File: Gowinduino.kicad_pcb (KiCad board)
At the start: 2 copper layers, 68.6 x 53.3 mm, 9 parts, among them J1 Power, J2 Analog, J3 Digital, J4 Digital, J5 SPI

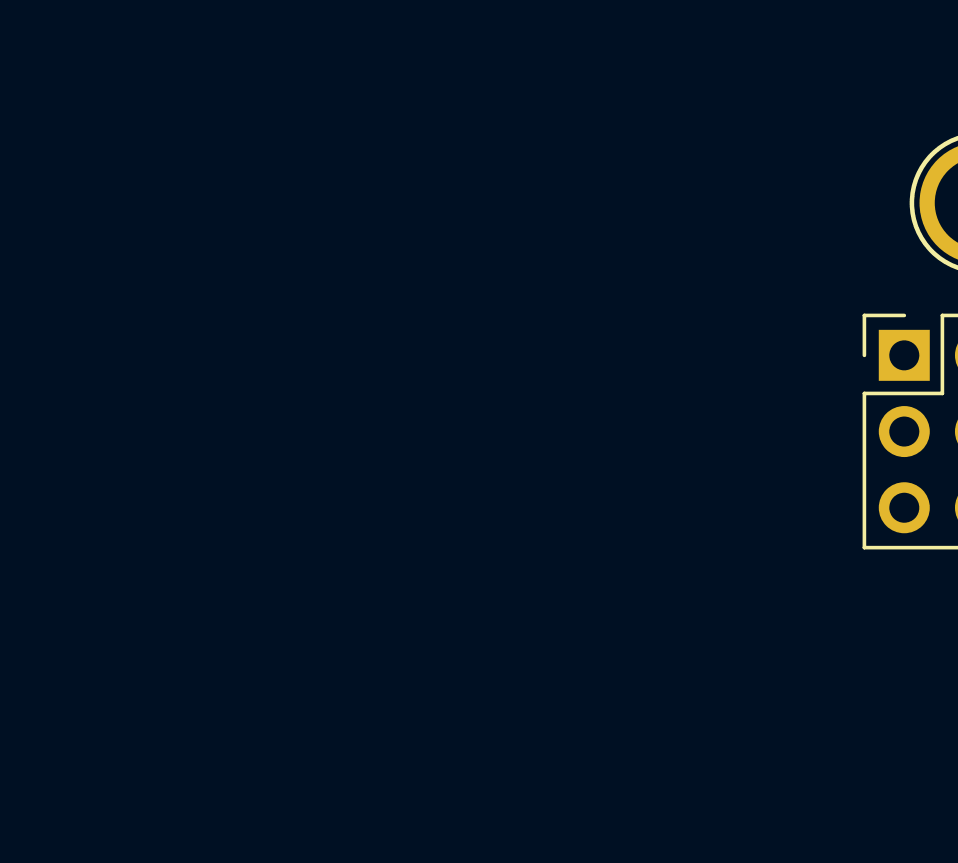
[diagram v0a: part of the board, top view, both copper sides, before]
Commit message: PCB: Introduced FPGA and SPI Flash
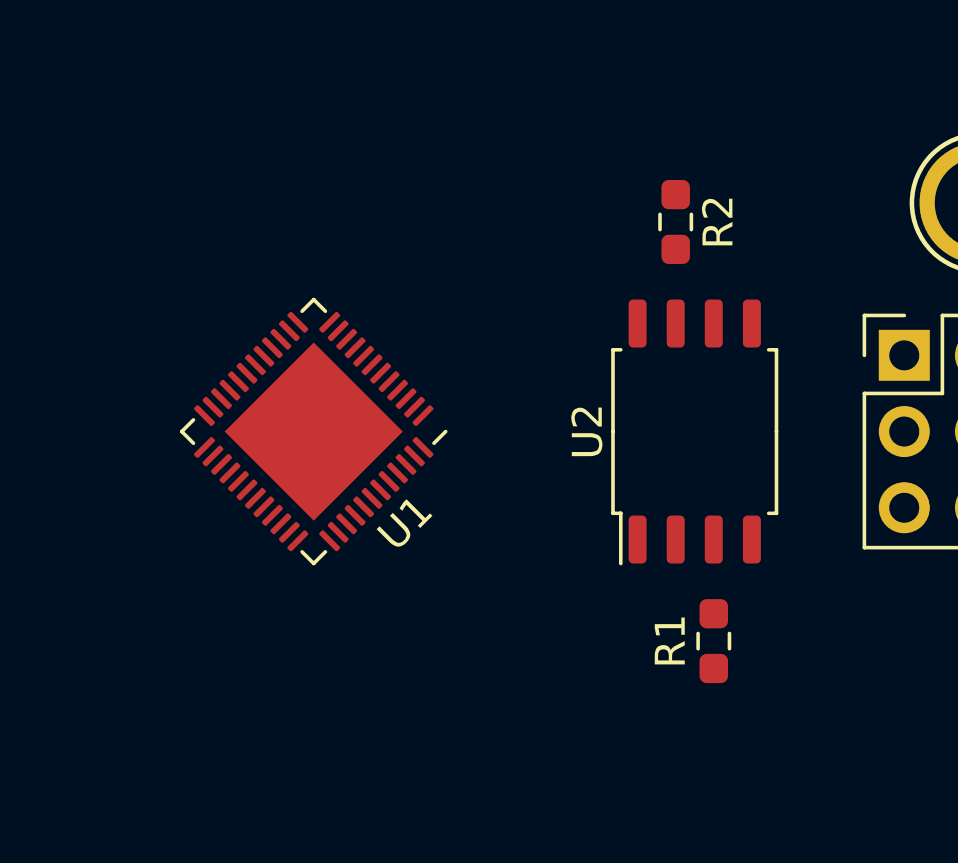
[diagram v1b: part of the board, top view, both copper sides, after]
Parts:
- added R1: 10k, Resistor_SMD:R_0603_1608Metric_Pad0.98x0.95mm_HandSolder, F.Cu at (168.1, 105.4)
- added R2: 10k, Resistor_SMD:R_0603_1608Metric_Pad0.98x0.95mm_HandSolder, F.Cu at (166.9, 91.4)
- added U1: GW1NSR-4CQN48P, Package_DFN_QFN:QFN-48-1EP_6x6mm_P0.4mm_EP4.2x4.2mm, F.Cu at (154.8, 98.4)
- added U2: W25Q32JVSS, Package_SO:SOIC-8_5.23x5.23mm_P1.27mm, F.Cu at (167.5, 98.4)
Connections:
- J5 pad 1: (no net) -> /MISO
- J5 pad 3: (no net) -> /SCLK
- J5 pad 4: (no net) -> /MOSI

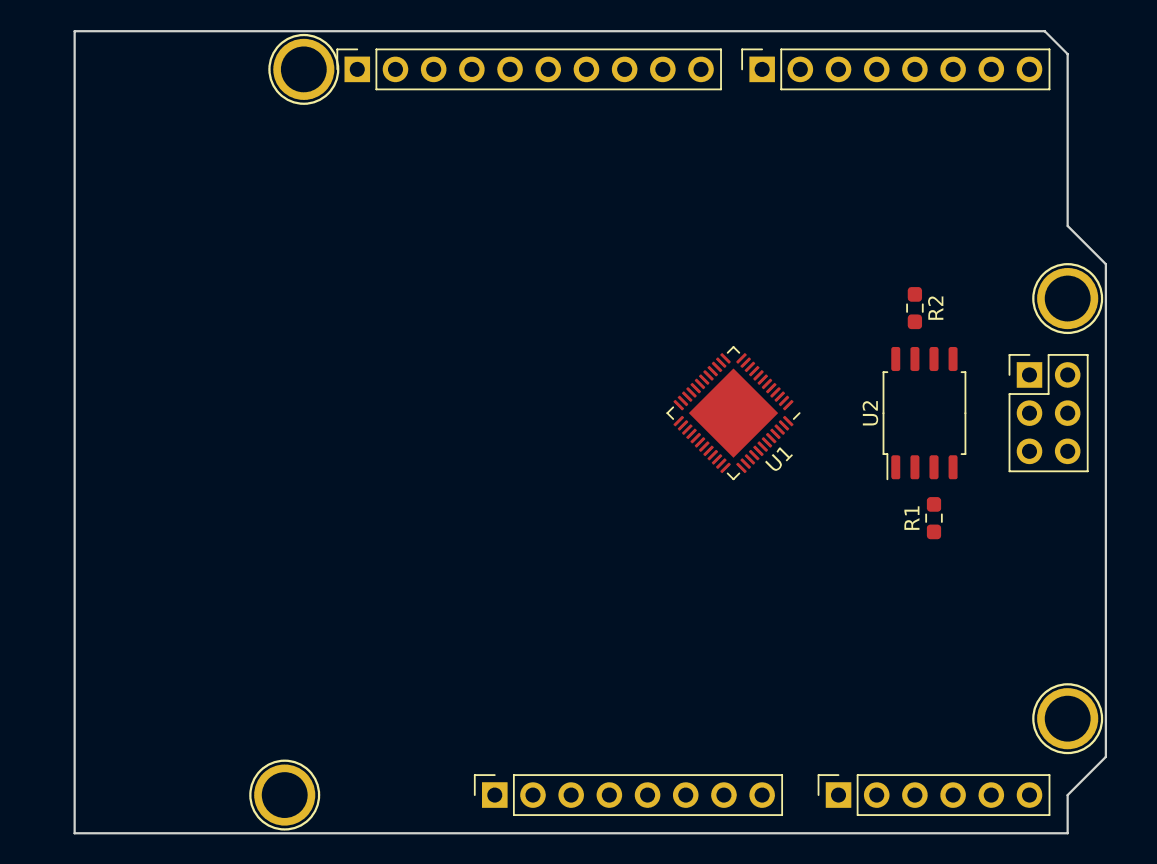
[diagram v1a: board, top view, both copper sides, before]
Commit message: Introduced JLCPCB DRC rules and GND fills
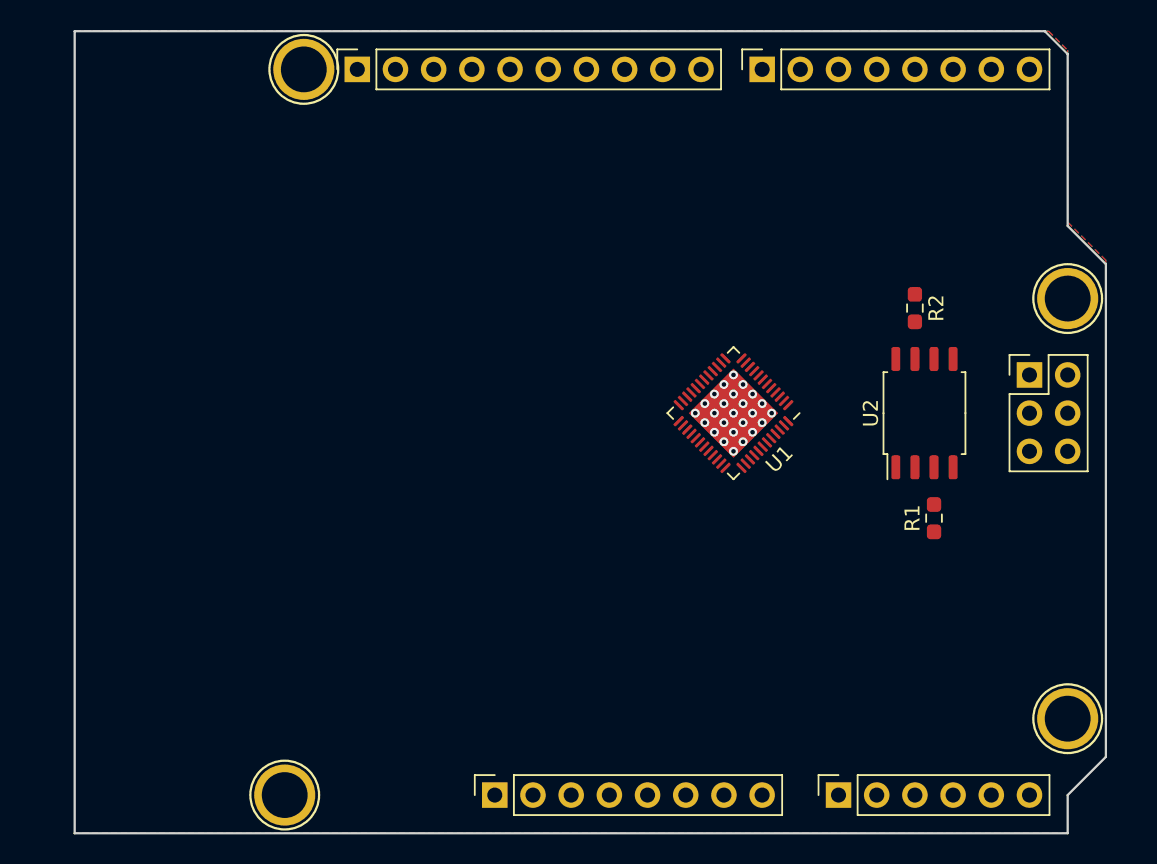
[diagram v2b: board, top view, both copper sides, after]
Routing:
- net GND: vias 0 -> 25
- added copper zone on B.Cu, net GND
- added copper zone on F.Cu, net GND
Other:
- net class Default: clearance 0.2 -> 0.127; trace_width 0.25 -> 0.127; via_drill 0.4 -> 0.3
- rule trace_clearance: 0.2 -> 0.127
- rule trace_min: 0.2 -> 0.127
- rule via_min_size: 0.4 -> 0.6
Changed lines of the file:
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@@
     (thickness 1.6)
     (drawings 26)
-    (tracks 0)
+    (tracks 25)
     (zones 0)
     (modules 13)
@@
   )
   (setup
-    (last_trace_width 0.25)
-    (trace_clearance 0.2)
+    (last_trace_width 0.127)
+    (user_trace_width 0.127)
+    (user_trace_width 0.1905)
+    (user_trace_width 0.254)
+    (user_trace_width 0.381)
+    (user_trace_width 0.508)
+    (trace_clearance 0.127)
     (zone_clearance 0.508)
     (zone_45_only no)
-    (trace_min 0.2)
+    (trace_min 0.127)
     (via_size 0.6)
-    (via_drill 0.4)
-    (via_min_size 0.4)
+    (via_drill 0.3)
+    (via_min_size 0.6)
     (via_min_drill 0.3)
     (uvia_size 0.3)
@@
   (net 12 /~CS)
   (net_class Default "This is the default net class."
-    (clearance 0.2)
-    (trace_width 0.25)
+    (clearance 0.127)
+    (trace_width 0.127)
     (via_dia 0.6)
-    (via_drill 0.4)
+    (via_drill 0.3)
     (uvia_dia 0.3)
     (uvia_drill 0.1)
-    (add_net +12V)
+    (diff_pair_width 0.127)
+    (diff_pair_gap 0.127)
     (add_net +1V2)
     (add_net +1V8)
     (add_net +3V3)
     (add_net +5V)
-    (add_net /0)
-    (add_net /1)
-    (add_net /10)
-    (add_net /11)
-    (add_net /12)
-    (add_net /13)
-    (add_net /14)
-    (add_net /15)
-    (add_net /2)
-    (add_net /3)
-    (add_net /4)
-    (add_net /5)
-    (add_net /6)
-    (add_net /7)
-    (add_net /8)
-    (add_net /9)
-    (add_net /A0)
-    (add_net /A1)
-    (add_net /A2)
-    (add_net /A3)
-    (add_net /A4)
-    (add_net /A5)
-    (add_net /AREF)
-    (add_net /DONE)
     (add_net /MISO)
     (add_net /MOSI)
     (add_net /SCLK)
-    (add_net /TCK)
-    (add_net /TDI)
-    (add_net /TDO)
-    (add_net /TMS)
     (add_net /~CS)
     (add_net /~RESET)
     (add_net GND)
-    (add_net "Net-(J1-Pad1)")
-    (add_net "Net-(PH1-Pad1)")
-    (add_net "Net-(PH2-Pad1)")
-    (add_net "Net-(PH3-Pad1)")
-    (add_net "Net-(PH4-Pad1)")
     (add_net "Net-(R1-Pad2)")
     (add_net "Net-(R2-Pad2)")
-    (add_net "Net-(U1-Pad10)")
-    (add_net "Net-(U1-Pad13)")
-    (add_net "Net-(U1-Pad14)")
-    (add_net "Net-(U1-Pad15)")
-    (add_net "Net-(U1-Pad16)")
-    (add_net "Net-(U1-Pad17)")
-    (add_net "Net-(U1-Pad18)")
-    (add_net "Net-(U1-Pad19)")
-    (add_net "Net-(U1-Pad20)")
-    (add_net "Net-(U1-Pad21)")
-    (add_net "Net-(U1-Pad22)")
-    (add_net "Net-(U1-Pad23)")
-    (add_net "Net-(U1-Pad27)")
-    (add_net "Net-(U1-Pad28)")
-    (add_net "Net-(U1-Pad29)")
-    (add_net "Net-(U1-Pad30)")
-    (add_net "Net-(U1-Pad31)")
-    (add_net "Net-(U1-Pad32)")
-    (add_net "Net-(U1-Pad33)")
-    (add_net "Net-(U1-Pad34)")
-    (add_net "Net-(U1-Pad35)")
-    (add_net "Net-(U1-Pad39)")
-    (add_net "Net-(U1-Pad40)")
-    (add_net "Net-(U1-Pad41)")
-    (add_net "Net-(U1-Pad42)")
-    (add_net "Net-(U1-Pad43)")
-    (add_net "Net-(U1-Pad44)")
-    (add_net "Net-(U1-Pad45)")
-    (add_net "Net-(U1-Pad46)")
-    (add_net "Net-(U1-Pad8)")
   )
   (module Package_SO:SOIC-8_5.23x5.23mm_P1.27mm (layer F.Cu)
@@
   (gr_line (start 120.523 82.55) (end 120.523 93.98) (angle 90) (layer Dwgs.User) (width 0.15))
   (gr_line (start 104.648 82.55) (end 120.523 82.55) (angle 90) (layer Dwgs.User) (width 0.15))
+  (via (at 154.813 97.155) (size 0.6) (drill 0.3) (layers F.Cu B.Cu) (net 2))
+  (via (at 155.448 97.79) (size 0.6) (drill 0.3) (layers F.Cu B.Cu) (net 2))
+  (via (at 156.083 98.425) (size 0.6) (drill 0.3) (layers F.Cu B.Cu) (net 2))
+  (via (at 155.448 99.06) (size 0.6) (drill 0.3) (layers F.Cu B.Cu) (net 2))
+  (via (at 154.813 99.695) (size 0.6) (drill 0.3) (layers F.Cu B.Cu) (net 2))
+  (via (at 154.178 99.06) (size 0.6) (drill 0.3) (layers F.Cu B.Cu) (net 2))
+  (via (at 153.543 98.425) (size 0.6) (drill 0.3) (layers F.Cu B.Cu) (net 2))
+  (via (at 152.908 97.79) (size 0.6) (drill 0.3) (layers F.Cu B.Cu) (net 2))
+  (via (at 152.273 98.425) (size 0.6) (drill 0.3) (layers F.Cu B.Cu) (net 2))
+  (via (at 152.908 99.06) (size 0.6) (drill 0.3) (layers F.Cu B.Cu) (net 2))
+  (via (at 153.543 99.695) (size 0.6) (drill 0.3) (layers F.Cu B.Cu) (net 2))
+  (via (at 154.178 100.33) (size 0.6) (drill 0.3) (layers F.Cu B.Cu) (net 2))
+  (via (at 154.813 100.965) (size 0.6) (drill 0.3) (layers F.Cu B.Cu) (net 2))
+  (via (at 155.448 100.33) (size 0.6) (drill 0.3) (layers F.Cu B.Cu) (net 2))
+  (via (at 156.083 99.695) (size 0.6) (drill 0.3) (layers F.Cu B.Cu) (net 2))
+  (via (at 156.718 99.06) (size 0.6) (drill 0.3) (layers F.Cu B.Cu) (net 2))
+  (via (at 157.353 98.425) (size 0.6) (drill 0.3) (layers F.Cu B.Cu) (net 2))
+  (via (at 156.718 97.79) (size 0.6) (drill 0.3) (layers F.Cu B.Cu) (net 2))
+  (via (at 156.083 97.155) (size 0.6) (drill 0.3) (layers F.Cu B.Cu) (net 2))
+  (via (at 155.448 96.52) (size 0.6) (drill 0.3) (layers F.Cu B.Cu) (net 2))
+  (via (at 154.813 95.885) (size 0.6) (drill 0.3) (layers F.Cu B.Cu) (net 2))
+  (via (at 154.178 96.52) (size 0.6) (drill 0.3) (layers F.Cu B.Cu) (net 2))
+  (via (at 153.543 97.155) (size 0.6) (drill 0.3) (layers F.Cu B.Cu) (net 2))
+  (via (at 154.178 97.79) (size 0.6) (drill 0.3) (layers F.Cu B.Cu) (net 2))
+  (via (at 154.813 98.425) (size 0.6) (drill 0.3) (layers F.Cu B.Cu) (net 2))
+  (zone (net 2) (net_name GND) (layer F.Cu) (hatch edge 0.508)
+    (connect_pads (clearance 0.1905))
+    (min_thickness 0.127)
+    (fill yes (arc_segments 32) (thermal_gap 0.1905) (thermal_bridge_width 0.381))
+    (polygon
+      (pts
+        (xy 177.038 74.295) (xy 177.038 85.725) (xy 179.578 88.265) (xy 179.578 121.285) (xy 177.038 123.825)
+        (xy 177.038 126.365) (xy 110.998 126.365) (xy 110.998 73.025) (xy 175.768 73.025)
+      )
+    )
+  )
+  (zone (net 2) (net_name GND) (layer B.Cu) (hatch edge 0.508)
+    (connect_pads (clearance 0.1905))
+    (min_thickness 0.127)
+    (fill yes (arc_segments 32) (thermal_gap 0.1905) (thermal_bridge_width 0.381))
+    (polygon
+      (pts
+        (xy 177.038 74.295) (xy 177.038 85.725) (xy 179.578 88.265) (xy 179.578 121.285) (xy 177.038 123.825)
+        (xy 177.038 126.365) (xy 110.998 126.365) (xy 110.998 73.025) (xy 175.768 73.025)
+      )
+    )
+  )
 )
